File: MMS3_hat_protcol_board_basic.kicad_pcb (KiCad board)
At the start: 2 copper layers, 100 x 50 mm, 30 parts, among them J1 Chainbus in, J11 Conn_01x04_Pin, J2 Chainbus Out, J3 Conn_01x04_Pin, J4 Conn_01x04_Pin, J7 Conn_01x06_Pin, U1 SN74CB3Q3384APW, U2 M24C64, U3 AMS1117

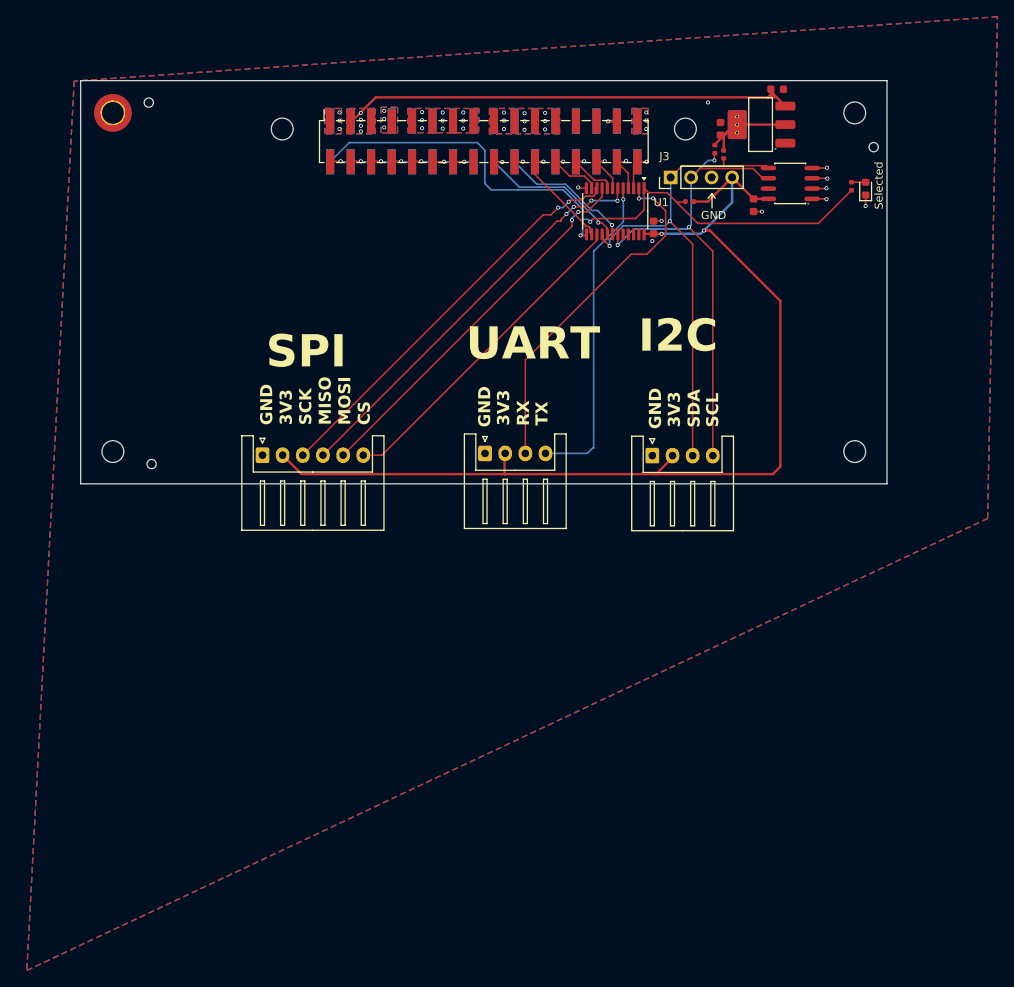
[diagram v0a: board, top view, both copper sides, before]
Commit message: updated routing, removed megamind
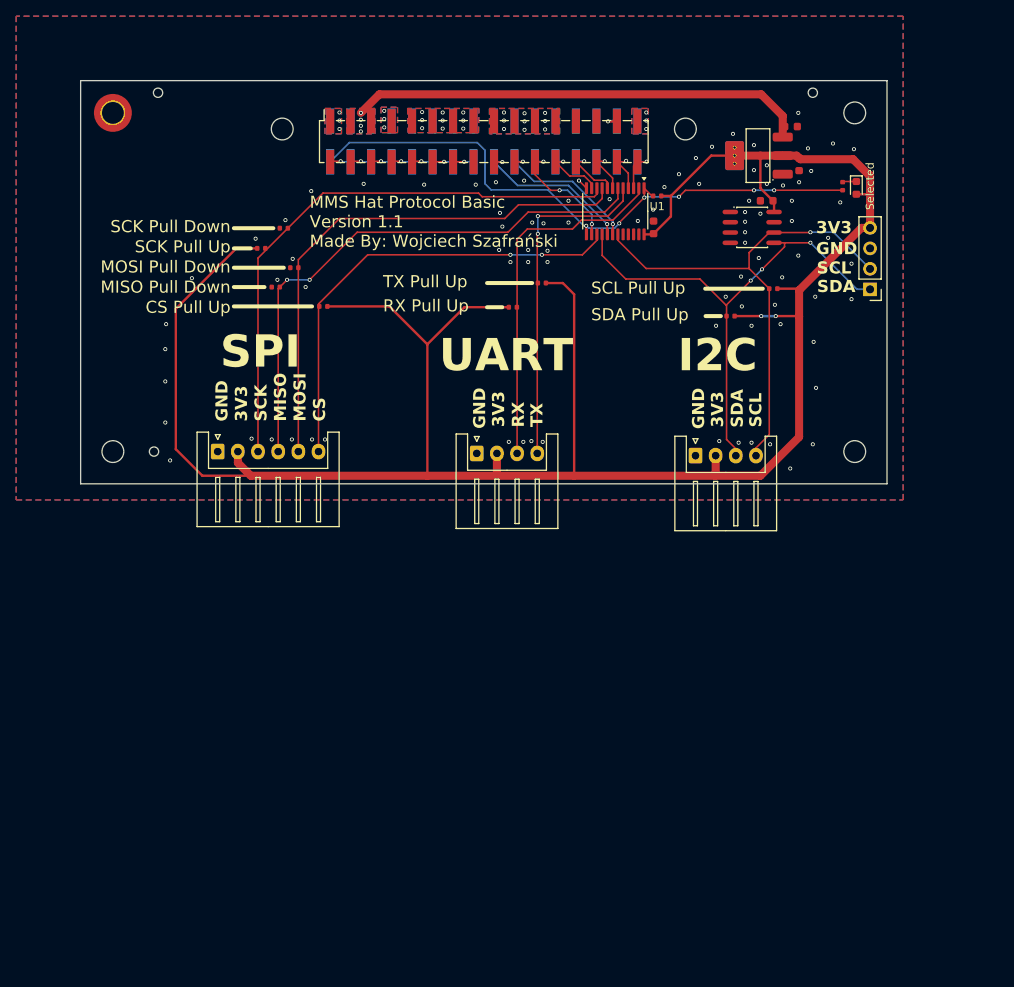
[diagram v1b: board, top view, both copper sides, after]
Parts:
- removed D1: LED, LED_SMD:LED_0603_1608Metric
- removed the G*** at (87.1, 118.8)
- removed PN1: ~, PCM_JLCPCB:Part_Num_JLCPCB
- added D3: Red, PCM_JLCPCB:D_0603, F.Cu at (174.2, 101.3)
- added R10: 10kΩ, PCM_JLCPCB:R_0402, F.Cu at (158.6, 117.2)
- added R11: 10kΩ, PCM_JLCPCB:R_0402, F.Cu at (104.5, 111.2)
- added R5: 10kΩ, PCM_JLCPCB:R_0402, F.Cu at (103.2, 106.3)
- added R6: 10kΩ, PCM_JLCPCB:R_0402, F.Cu at (163.9, 113.8)
- added R7: 10kΩ, PCM_JLCPCB:R_0402, F.Cu at (135.2, 113.1)
- added R8: 10kΩ, PCM_JLCPCB:R_0402, F.Cu at (131.6, 116.1)
- added R9: 10kΩ, PCM_JLCPCB:R_0402, F.Cu at (102.2, 113.6)
- moved R3 58.5 mm to (100.4, 108.8), turned to 0 degrees
- moved R2 52.3 mm to (108.1, 116.0), turned to 180 degrees
- moved J3 28.4 mm to (175.9, 113.9), turned to 180 degrees
- moved G*** 19.6 mm to (96.8, 99.5)
- moved C4 10.7 mm to (167.1, 98.4), turned to -90 degrees
- moved H8 10.1 mm to (168.8, 89.5)
- moved U2 7.21 mm to (161.3, 106.2), turned to -90 degrees
- moved J7 5.57 mm to (95.0, 134.0)
- moved J4 5.35 mm to (154.2, 134.5)
- moved C3 4.94 mm to (166.1, 93.7)
- moved R4 4.06 mm to (149.5, 102.3)
- moved U3 3.86 mm to (162.1, 97.3)
- moved C2 1.72 mm to (163.1, 102.9), turned to 180 degrees
- moved H9 1.68 mm to (87.6, 89.5)
- moved H7 1.58 mm to (87.1, 134.0)
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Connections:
- R2 pad 2: /Chainbus.SCL -> /Chainbus.CS
- R3 pad 2: /Chainbus.SDA -> /Chainbus.SCK
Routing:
- net +3V3: track 141.7 -> 282.2 mm
- net /Chainbus.SCK: track 50.7 -> 70.4 mm, vias 2 -> 0
- net /Chainbus.MOSI: track 47.0 -> 65.9 mm, vias 2 -> 0
- net /Chainbus.MISO: track 51.3 -> 68.3 mm, vias 4 -> 2
- net /Chainbus.CS: track 40.8 -> 56.8 mm, vias 0 -> 2
- net GND: track 12.1 -> 1.32 mm, vias 28 -> 108
- net /Bus_switch/SEL1: track 83.6 -> 77.3 mm, vias 2 -> 6
- net /Chainbus.SDA: track 60.5 -> 64.6 mm, vias 2 -> 3
- net /Chainbus.TX: track 40.0 -> 42.4 mm, vias 1 -> 2
- net /Chainbus.SCL: track 61.4 -> 63.3 mm, vias 3 -> 1
- net +5V: track 58.2 -> 57.0 mm
- net /Bus_switch/Chainbus_In.CS: track 14.2 -> 15.3 mm, vias 1 -> 3
- net /Chainbus.RX: track 43.7 -> 44.7 mm, vias 2 -> 0
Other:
- board text added: "CS Pull Up"
- board text added: "DEVICE ESD SENSITIVE"
- board text added: "Front and Back keepout zone for DIN rail mount"
- board text added: "MISO Pull Down"
- board text added: "MMS Hat Protocol Basic Version 1.1 Made By: Wojciech Szafrański"
- board text added: "MOSI Pull Down"
- board text added: "RX Pull Up"
- board text added: "SCK Pull Down"
- board text added: "SCK Pull Up"
- board text added: "SCL Pull Up"
- board text added: "SDA Pull Up"
- board text added: "TX Pull Up"
- board text added: "This is prototype device It is not certified according to current EU laws. Do not sell or use outside of research purposes."
- board text removed: "ASS DEVICE"
- board text removed: "DONT USE IN PROJECTS PLEASE ONLY FOR TESTING PURPOSES USE NORMAL PROTOCOL BOARD"
